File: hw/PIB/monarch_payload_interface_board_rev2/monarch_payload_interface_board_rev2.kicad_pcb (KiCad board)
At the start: 4 copper layers, 96 x 89.9 mm, 226 parts, among them J1 2200980271, J13 2200980471, J14 2200980471, J15 2200980471, J16 2200980271, J17 Conn_02x04_Counter_Clockwise, J18 2200980671, J19 2200980671, J2 Conn_01x06, J20 2200980671, J21 2200980671, J22 2200980671, J23 2200980671, J24 2200980671, J25 2200980471, J3 Conn_01x05, J4 Conn_01x04, J5 Conn_01x05, J6 2200980671, J8 2200980671, Q1 FZT600TA, Q10 FZT600TA, Q11 FZT600TA, Q12 FZT600TA, Q13 FZT600TA, Q14 FZT600TA, Q15 FZT600TA, Q16 FZT600TA, Q17 FZT600TA, Q18 FZT600TA, Q19 FZT600TA, Q2 FZT600TA, Q3 FZT600TA, Q4 FZT600TA, Q5 FZT600TA, Q6 FZT600TA, Q7 FZT600TA, Q8 FZT600TA, Q9 FZT600TA, SW1 SW_BOOT, SW2 SW_RESET, U1 Payload, U10 AD7124-8BCPZ-RL, U11 WSK06121L000FEA, U12 WSK06121L000FEA, U13 WSK06121L000FEA, U14 WSK06121L000FEA, U2 STM32L4A6VGTx, U3 MAX31856MUD_T, U4 TPS61088QRHLRQ1, U5 MAX31856MUD_T, U6 MAX31856MUD_T, U7 MAX31856MUD_T, U8 MAX31856MUD_T, U9 AD7124-8BCPZ-RL

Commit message: PIB Rev Done -> Review Awaiting + DRC Check
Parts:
- moved D4 6.56 mm to (50.5, 69.8), turned to 90 degrees
- moved D2 5.41 mm to (52.0, 69.8), turned to 90 degrees
- moved R58 4.28 mm to (50.5, 66.8), turned to 90 degrees
- moved R57 2.21 mm to (52.0, 66.8), turned to 90 degrees
- moved R56 2.00 mm to (52.0, 63.5), turned to -90 degrees
- moved D3 1.89 mm to (50.5, 63.5), turned to 90 degrees
- moved R38 1.88 mm to (90.2, 28.1)
- moved SW2 1.54 mm to (51.0, 72.5), turned to -90 degrees
- moved C46 0.85 mm to (97.0, 41.1)
- moved C76 0.40 mm to (92.7, 30.0)
- moved R66 0.05 mm to (92.0, 41.9)
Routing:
- net 12VA_VA-: track 398.5 -> 410.3 mm, vias 123 -> 121
- net +3V3: track 214.9 -> 219.0 mm, vias 22 -> 23
- net /MCU/GREEN_LED: track 2.16 -> 5.77 mm
- net /MCU/RED_LED: track 1.93 -> 4.14 mm
- net /MCU/NRST: track 67.4 -> 69.4 mm
- net /Connectors/SPI2_SCK: track 109.5 -> 108.4 mm
- net /MCU/BLUE_LED: track 3.07 -> 3.82 mm
- net Net-(U9-REGCAPD): track 2.13 -> 2.87 mm

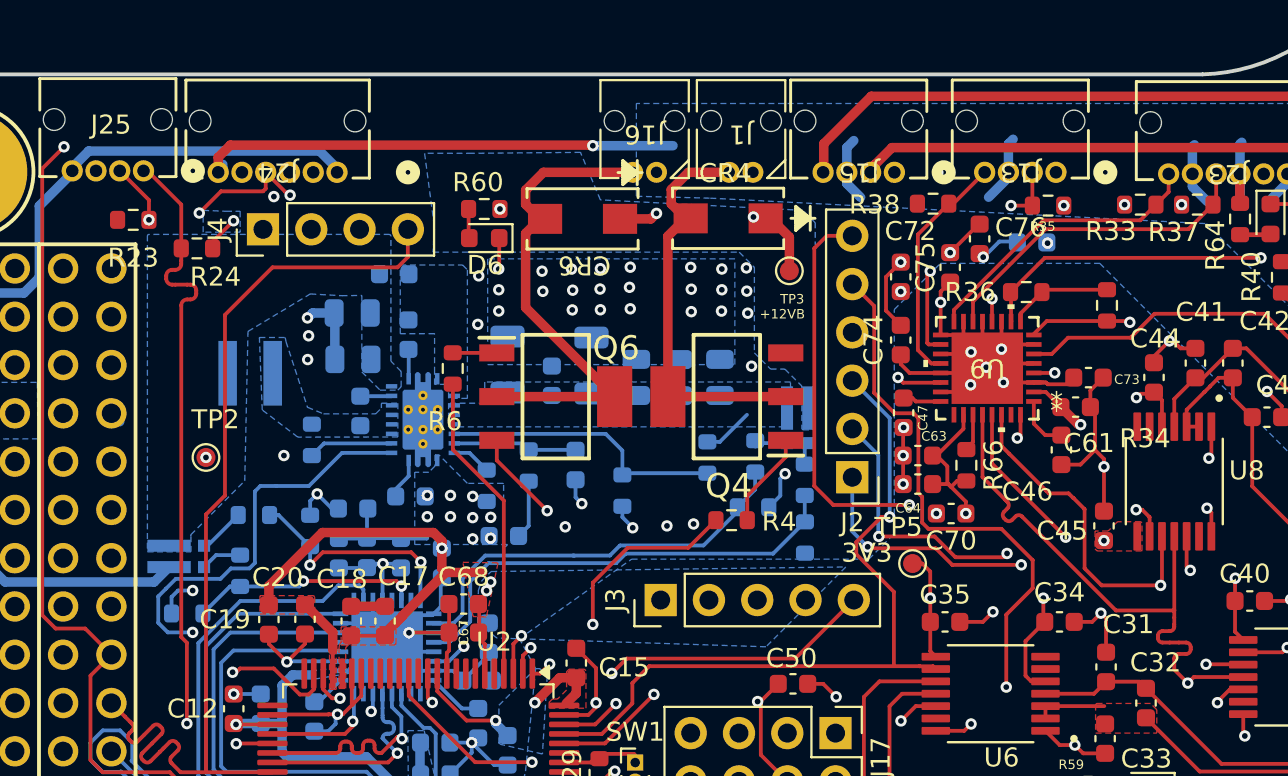
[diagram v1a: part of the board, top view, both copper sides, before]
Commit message: DRC Fixes such as VIAs
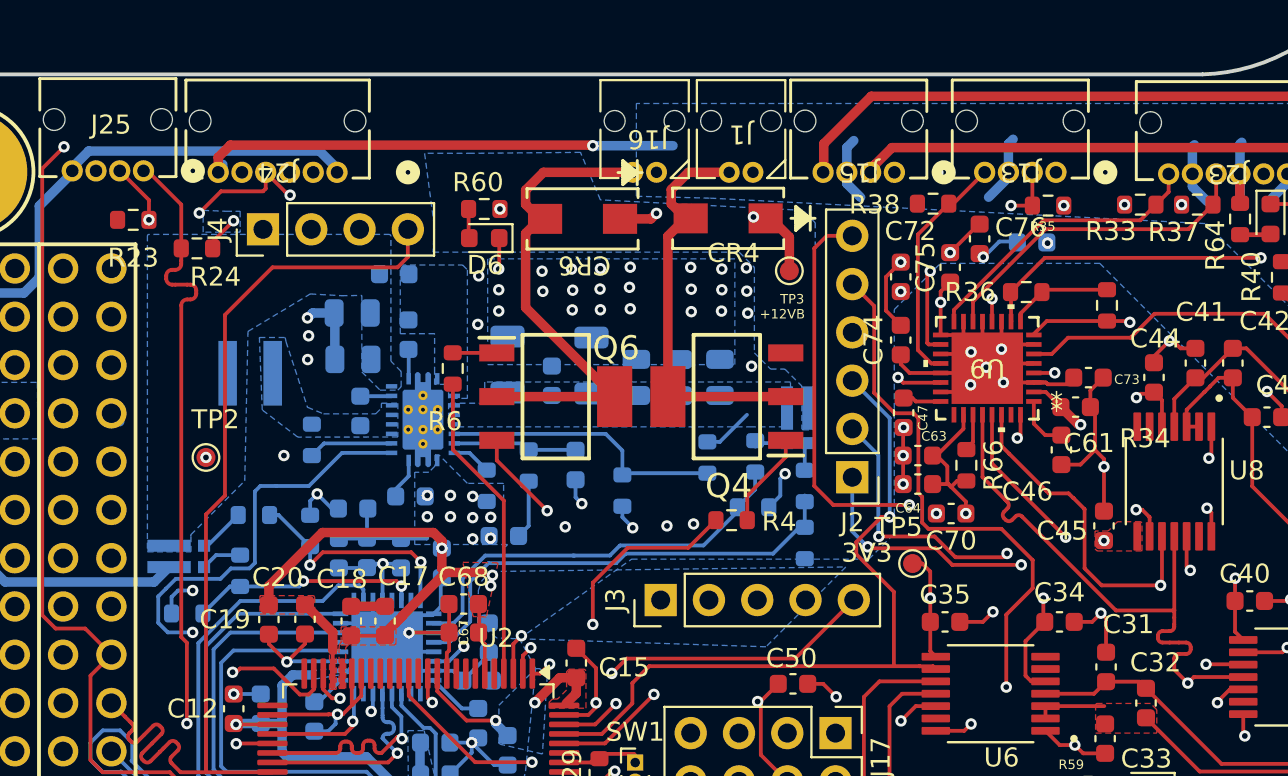
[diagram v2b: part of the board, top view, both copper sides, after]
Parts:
- moved R48 0.33 mm to (83.5, 43.0)
- moved R55 0.29 mm to (83.5, 46.0)
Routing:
- net /Connectors/UART_PPU_TX: track 43.4 -> 43.7 mm, vias 2 -> 1
- net P5REF+: vias 1 -> 0
- net /Connectors/I2C4_SDA: vias 3 -> 2
- net /Connectors/I2C4_SCL: vias 3 -> 2
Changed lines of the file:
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@@
 		(tags "LQFP QFP")
 		(property "Reference" "U2"
-			(at -9.345 -3.98 180)
+			(at -9.545 -4.08 180)
 			(layer "F.SilkS")
 			(effects
@@
 		(tags "S1J-13-F ")
 		(property "Reference" "CR4"
-			(at 0.1499 2.37 0)
+			(at -0.28 -1.83 0)
 			(unlocked yes)
 			(layer "F.SilkS")
@@
 		(tags "2200980271")
 		(property "Reference" "J16"
-			(at 0 0 180)
+			(at -0.175 -0.25 180)
 			(unlocked yes)
 			(layer "F.SilkS")
@@
 		(tags "capacitor")
 		(property "Reference" "C87"
-			(at 0 1.43 90)
+			(at 0 1.62 90)
 			(layer "B.SilkS")
 			(effects
@@
 	(footprint "Resistor_SMD:R_0603_1608Metric"
 		(layer "B.Cu")
-		(at 83.51 45.71 90)
+		(at 83.5 46 90)
 		(descr "Resistor SMD 0603 (1608 Metric), square (rectangular) end terminal, IPC-7351 nominal, (Body size source: IPC-SM-782 page 72, https://www.pcb-3d.com/wordpress/wp-content/uploads/ipc-sm-782a_amendment_1_and_2.pdf), generated with kicad-footprint-generator")
 		(tags "resistor")
@@
 			(at -0.275 1.67 0)
 			(layer "B.SilkS")
+			(hide yes)
 			(effects
 				(font
@@
 	(footprint "Resistor_SMD:R_0603_1608Metric"
 		(layer "B.Cu")
-		(at 83.5 42.675 90)
+		(at 83.5 43 90)
 		(descr "Resistor SMD 0603 (1608 Metric), square (rectangular) end terminal, IPC-7351 nominal, (Body size source: IPC-SM-782 page 72, https://www.pcb-3d.com/wordpress/wp-content/uploads/ipc-sm-782a_amendment_1_and_2.pdf), generated with kicad-footprint-generator")
 		(tags "resistor")
@@
 	)
 	(segment
+		(start 66.375 51.03)
+		(end 66.375 49.25)
+		(width 0.2)
+		(layer "F.Cu")
+		(net "+3V3")
+	)
+	(segment
 		(start 63.97 45.45)
 		(end 58.119339 45.45)
@@
 	)
 	(segment
+		(start 66.67 52.87)
+		(end 66.67 51.325)
+		(width 0.2)
+		(layer "F.Cu")
+		(net "+3V3")
+	)
+	(segment
 		(start 94.45 59.45)
 		(end 94.4375 59.4625)
@@
 	)
 	(segment
+		(start 66.67 51.325)
+		(end 66.375 51.03)
+		(width 0.2)
+		(layer "F.Cu")
+		(net "+3V3")
+	)
+	(segment
 		(start 53.58 55.545)
 		(end 55.495 55.545)
@@
 	)
 	(segment
-		(start 66.67 51.325)
-		(end 66.375 51.03)
-		(width 0.2)
-		(layer "F.Cu")
-		(net "+3V3")
-	)
-	(segment
 		(start 95.5003 38.0549)
 		(end 96.1799 38.0549)
@@
 	)
 	(segment
+		(start 66.375 49.25)
+		(end 66.335 49.21)
+		(width 0.2)
+		(layer "F.Cu")
+		(net "+3V3")
+	)
+	(segment
 		(start 110.66853 60.4)
 		(end 111.085 60.4)
@@
 	)
 	(segment
-		(start 66.375 51.03)
-		(end 66.375 49.49)
-		(width 0.2)
-		(layer "F.Cu")
-		(net "+3V3")
-	)
-	(segment
 		(start 52.35 30.15)
 		(end 53.45 29.05)
@@
 	)
 	(segment
-		(start 66.67 52.87)
-		(end 66.67 51.325)
-		(width 0.2)
-		(layer "F.Cu")
-		(net "+3V3")
-	)
-	(segment
 		(start 89.68 47.08)
 		(end 89.17 47.08)
@@
 	)
 	(via
-		(at 66.76 48.51)
+		(at 67.07 47.698528)
 		(size 0.6)
 		(drill 0.3)
@@
 	)
 	(via
-		(at 66.98 48.05)
+		(at 66.98 48.25)
 		(size 0.6)
 		(drill 0.3)
@@
 	)
 	(via
-		(at 55.571529 27.776958)
-		(size 0.6)
-		(drill 0.3)
-		(layers "F.Cu" "B.Cu")
-		(capping no)
-		(covering
-			(front no)
-			(back no)
-		)
-		(plugging
-			(front no)
-			(back no)
-		)
-		(filling no)
-		(net "/Connectors/UART_PPU_TX")
-	)
-	(via
 		(at 53.4 52.8)
 		(size 0.6)
@@
 	)
 	(segment
-		(start 51.981485 52.8)
-		(end 51.672165 52.49068)
-		(width 0.2)
-		(layer "In1.Cu")
-		(net "/Connectors/UART_PPU_TX")
-	)
-	(segment
-		(start 55.443042 27.776958)
-		(end 55.37 27.85)
+		(start 49.7 30.799943)
+		(end 49.7 50.518515)
 		(width 0.2)
 		(layer "In1.Cu")
@@
 	)
 	(segment
-		(start 55.571529 27.778471)
-		(end 55 28.35)
+		(start 51.981485 52.8)
+		(end 51.672165 52.49068)
 		(width 0.2)
 		(layer "In1.Cu")
@@
 	)
 	(segment
-		(start 55.571529 27.776958)
-		(end 55.571529 27.708471)
+		(start 55.5 27.85)
+		(end 55.5 27.3931)
 		(width 0.2)
 		(layer "In1.Cu")
@@
 	)
 	(segment
-		(start 51.5329 27.85)
-		(end 49.699 29.6839)
-		(width 0.2)
-		(layer "In1.Cu")
-		(net "/Connectors/UART_PPU_TX")
-	)
-	(segment
 		(start 51.332753 52.49068)
 		(end 51.184259 52.639171)
@@
 	)
 	(segment
-		(start 55.571529 27.776958)
-		(end 55.443042 27.776958)
+		(start 50.908488 51.727003)
+		(end 50.823636 51.642151)
 		(width 0.2)
 		(layer "In1.Cu")
@@
 	)
 	(segment
-		(start 49.699 30.798943)
-		(end 49.7 30.799943)
+		(start 55 28.35)
+		(end 55.5 27.85)
 		(width 0.2)
 		(layer "In1.Cu")
@@
 	)
 	(segment
-		(start 50.908488 51.727003)
-		(end 50.823636 51.642151)
+		(start 49.911467 51.366378)
+		(end 50.059958 51.217884)
 		(width 0.2)
 		(layer "In1.Cu")
@@
 	)
 	(segment
-		(start 49.7 30.799943)
-		(end 49.7 50.518515)
+		(start 49.975107 50.793622)
+		(end 49.802252 50.620767)
 		(width 0.2)
 		(layer "In1.Cu")
@@
 	)
 	(segment
-		(start 49.911467 51.366378)
-		(end 50.059958 51.217884)
-		(width 0.2)
-		(layer "In1.Cu")
-		(net "/Connectors/UART_PPU_TX")
-	)
-	(segment
-		(start 55.571529 27.776958)
-		(end 55.571529 27.778471)
+		(start 50.484224 51.642151)
+		(end 50.33573 51.790642)
 		(width 0.2)
 		(layer "In1.Cu")
@@
 	)
 	(segment
-		(start 49.975107 50.793622)
-		(end 49.802252 50.620767)
+		(start 56.3931 26.8869)
+		(end 56.3931 26.5)
 		(width 0.2)
 		(layer "In1.Cu")
@@
 	)
 	(segment
-		(start 50.484224 51.642151)
-		(end 50.33573 51.790642)
+		(start 55.5 27.85)
+		(end 51.5329 27.85)
 		(width 0.2)
 		(layer "In1.Cu")
@@
 	)
 	(segment
-		(start 55.37 27.85)
-		(end 51.5329 27.85)
+		(start 49.699 30.798943)
+		(end 49.7 30.799943)
 		(width 0.2)
 		(layer "In1.Cu")
@@
 	)
 	(segment
-		(start 55.571529 27.708471)
-		(end 56.3931 26.8869)
+		(start 55.5 27.3931)
+		(end 56.3931 26.5)
 		(width 0.2)
 		(layer "In1.Cu")
@@
 	)
 	(segment
-		(start 56.3931 26.8869)
-		(end 56.3931 26.5)
+		(start 51.5329 27.85)
+		(end 49.699 29.6839)
 		(width 0.2)
 		(layer "In1.Cu")
@@
 	)
 	(via
-		(at 48.7146 26.4238)
-		(size 0.6)
-		(drill 0.3)
-		(layers "F.Cu" "B.Cu")
-		(capping no)
-		(covering
-			(front no)
-			(back no)
-		)
-		(plugging
-			(front no)
-			(back no)
-		)
-		(filling no)
-		(net "/Connectors/I2C4_SDA")
-	)
-	(via
 		(at 50.997 55.5)
 		(size 0.6)
@@
 		(net "/Connectors/I2C4_SCL")
 	)
-	(via
-		(at 47.4646 26.4238)
-		(size 0.6)
-		(drill 0.3)
-		(layers "F.Cu" "B.Cu")
-		(capping no)
-		(covering
-			(front no)
-			(back no)
-		)
-		(plugging
-			(front no)
-			(back no)
-		)
-		(filling no)
-		(net "/Connectors/I2C4_SCL")
-	)
 	(segment
 		(start 47.435001 26.25)
@@
 		(net "P5REF+")
 	)
-	(via
-		(at 102.6431 26.5842)
-		(size 0.6)
-		(drill 0.3)
-		(layers "F.Cu" "B.Cu")
-		(capping no)
-		(covering
-			(front no)
-			(back no)
-		)
-		(plugging
-			(front no)
-			(back no)
-		)
-		(filling no)
-		(net "P5REF+")
-	)
 	(segment
 		(start 91.948 41.085)
@@
 	)
 	(segment
-		(start 83.5 45)
-		(end 83.5 43.5)
+		(start 81.835 46.56)
+		(end 83.22 45.175)
 		(width 0.2)
 		(layer "B.Cu")
@@
 	)
 	(segment
-		(start 63.9826 51.2231)
-		(end 64.8069 51.2231)
+		(start 65.9 48.02)
+		(end 66.86 47.06)
 		(width 0.2)
 		(layer "B.Cu")
@@
 	)
 	(segment
-		(start 73.58 47.06)
-		(end 74.08 46.56)
+		(start 66.86 47.06)
+		(end 73.58 47.06)
 		(width 0.2)
 		(layer "B.Cu")
@@
 	)
 	(segment
-		(start 81.835 46.56)
-		(end 83.51 44.885)
+		(start 64.8069 51.2231)
+		(end 65.9 50.13)
+		(width 0.2)
+		(layer "B.Cu")
+		(net "12VB_VB+")
+	)
+	(segment
+		(start 63.9826 51.2231)
+		(end 64.8069 51.2231)
 		(width 0.2)
 		(layer "B.Cu")
@@
 	)
 	(segment
-		(start 65.9 48.02)
-		(end 66.86 47.06)
+		(start 83.22 45.175)
+		(end 83.5 45.175)
 		(width 0.2)
 		(layer "B.Cu")
@@
 	)
 	(segment
-		(start 66.86 47.06)
-		(end 73.58 47.06)
+		(start 73.58 47.06)
+		(end 74.08 46.56)
 		(width 0.2)
 		(layer "B.Cu")
@@
 	)
 	(segment
-		(start 64.8069 51.2231)
-		(end 65.9 50.13)
+		(start 83.5 45)
+		(end 83.5 43.5)
 		(width 0.2)
 		(layer "B.Cu")
@@
 	)
 	(segment
-		(start 83.5 41.85)
+		(start 83.5 42.175)
 		(end 83.5 40.930111)
 		(width 0.2)

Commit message: FINAL REVIEW DONE + A lot of fixes. DRC PASSED
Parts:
- added J7: Conn_01x02, Connector_PPU:CONN02_534260210_MOL, F.Cu at (116.1, 42.3)
- moved R24 8.39 mm to (50.0, 38.8), turned to 0 degrees
- moved J22 6.70 mm to (120.3, 53.6)
- moved TP2 4.75 mm to (52.0, 36.8)
- moved R31 4.10 mm to (117.8, 35.5), turned to 90 degrees
- moved J14 3.48 mm to (120.4, 61.7)
- moved R39 3.00 mm to (118.5, 50.0), turned to -90 degrees
- moved R32 2.95 mm to (118.7, 47.0), turned to -90 degrees
- moved Q18 2.74 mm to (122.2, 31.8)
- moved J4 1.83 mm to (53.2, 29.2)
- moved C20 0.46 mm to (56.8, 50.0)
- moved J19 0.32 mm to (51.4, 100.2)
- moved J18 0.31 mm to (120.2, 85.4)
- moved C19 0.31 mm to (55.0, 50.0)
- moved J20 0.19 mm to (65.1, 100.2)
- moved J6 0.18 mm to (94.3, 100.2)
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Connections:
- net /USART3_RX renamed /Connectors/USART3_RX
- net /USART3_TX renamed /Connectors/USART3_TX
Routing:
- net +3V3: track 219.3 -> 238.2 mm
- net 12VA_VA-: track 410.3 -> 424.4 mm, vias 121 -> 128
- net P1REF+: track 29.7 -> 35.9 mm
- net P2REF+: track 27.8 -> 34.1 mm
- net P0REF+: track 29.0 -> 34.5 mm
- net /MCU/Valve18: track 80.8 -> 85.3 mm
- net /Connectors/T3-: track 9.20 -> 12.8 mm
- net /Connectors/T3+: track 11.5 -> 15.1 mm
- net /Connectors/T4-: track 31.3 -> 34.2 mm
- net +12VA: track 51.8 -> 54.6 mm, vias 67 -> 66
- net /Connectors/T4+: track 32.8 -> 35.1 mm
- net /Connectors/Valve18-: track 55.4 -> 53.3 mm
- net /Connectors/USART3_TX: track 52.8 -> 54.7 mm
- net /Connectors/T2-: track 32.7 -> 31.6 mm
- net /Connectors/T2+: track 33.3 -> 32.3 mm
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- added copper zone on F.Cu, net 12VA_VA-
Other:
- board text added: "VBAT"

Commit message: Final Changes
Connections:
- R29 pad 2: unconnected-(R29-Pad2) -> Net-(U2-PH3)
- SW1 pad 1: unconnected-(R29-Pad2) -> Net-(U2-PH3)
- U2 pad 94: unconnected-(R29-Pad2) -> Net-(U2-PH3)
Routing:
- net unconnected-(R29-Pad2): track 3.95 -> 0.00 mm
- net Net-(U2-PH3): track 0.00 -> 3.90 mm
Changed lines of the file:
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@@
 			(layers "*.Cu" "*.Mask")
 			(remove_unused_layers no)
-			(net "unconnected-(R29-Pad2)")
+			(net "Net-(U2-PH3)")
 			(pinfunction "1_1")
 			(pintype "passive")
@@
 			(layers "F.Cu" "F.Mask" "F.Paste")
 			(roundrect_rratio 0.25)
-			(net "unconnected-(R29-Pad2)")
+			(net "Net-(U2-PH3)")
 			(pinfunction "PH3_94")
 			(pintype "bidirectional")
@@
 			(layers "F.Cu" "F.Mask" "F.Paste")
 			(roundrect_rratio 0.25)
-			(net "unconnected-(R29-Pad2)")
+			(net "Net-(U2-PH3)")
 			(pintype "passive")
 		)
@@
 	)
 	(gr_text "+12VB\n"
-		(at 82 34.25 0)
+		(at 82.55 34.2 0)
 		(layer "F.SilkS")
 		(effects
@@
 	)
 	(segment
+		(start 73.06 57.45)
+		(end 76.17 54.34)
+		(width 0.2)
+		(layer "In1.Cu")
+		(net "/MCU/NRST")
+	)
+	(segment
 		(start 69.15 57.53)
-		(end 72.98 57.53)
+		(end 69.23 57.45)
 		(width 0.2)
 		(layer "In1.Cu")
@@
 	)
 	(segment
-		(start 72.98 57.53)
-		(end 76.17 54.34)
+		(start 69.23 57.45)
+		(end 73.06 57.45)
 		(width 0.2)
 		(layer "In1.Cu")
@@
 	)
 	(segment
-		(start 74.515 57.095)
-		(end 74.58 57.16)
-		(width 0.2)
-		(layer "F.Cu")
-		(net "unconnected-(R29-Pad2)")
-	)
-	(segment
-		(start 72.25 57.545)
-		(end 70.845 57.545)
-		(width 0.2)
-		(layer "F.Cu")
-		(net "unconnected-(R29-Pad2)")
-	)
-	(segment
-		(start 72.7 57.095)
-		(end 74.515 57.095)
-		(width 0.2)
-		(layer "F.Cu")
-		(net "unconnected-(R29-Pad2)")
-	)
-	(segment
-		(start 72.7 57.095)
-		(end 72.25 57.545)
-		(width 0.2)
-		(layer "F.Cu")
-		(net "unconnected-(R29-Pad2)")
-	)
-	(segment
 		(start 72.32 25.07)
 		(end 53.282838 25.07)
@@
 		(net "/Connectors/USART3_RX")
 	)
+	(segment
+		(start 73.729143 57.473)
+		(end 73.801143 57.545)
+		(width 0.2)
+		(layer "F.Cu")
+		(net "Net-(U2-PH3)")
+	)
+	(segment
+		(start 74.195 57.545)
+		(end 74.2 57.55)
+		(width 0.2)
+		(layer "F.Cu")
+		(net "Net-(U2-PH3)")
+	)
+	(segment
+		(start 72.5 57.545)
+		(end 72.7 57.345)
+		(width 0.2)
+		(layer "F.Cu")
+		(net "Net-(U2-PH3)")
+	)
+	(segment
+		(start 73.164561 57.345)
+		(end 73.292561 57.473)
+		(width 0.2)
+		(layer "F.Cu")
+		(net "Net-(U2-PH3)")
+	)
+	(segment
+		(start 74.2 57.55)
+		(end 74.58 57.55)
+		(width 0.2)
+		(layer "F.Cu")
+		(net "Net-(U2-PH3)")
+	)
+	(segment
+		(start 73.292561 57.473)
+		(end 73.729143 57.473)
+		(width 0.2)
+		(layer "F.Cu")
+		(net "Net-(U2-PH3)")
+	)
+	(segment
+		(start 73.801143 57.545)
+		(end 74.195 57.545)
+		(width 0.2)
+		(layer "F.Cu")
+		(net "Net-(U2-PH3)")
+	)
+	(segment
+		(start 70.845 57.545)
+		(end 72.5 57.545)
+		(width 0.2)
+		(layer "F.Cu")
+		(net "Net-(U2-PH3)")
+	)
+	(segment
+		(start 72.7 57.345)
+		(end 73.164561 57.345)
+		(width 0.2)
+		(layer "F.Cu")
+		(net "Net-(U2-PH3)")
+	)
 	(zone
